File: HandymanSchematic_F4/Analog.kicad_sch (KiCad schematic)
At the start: 43 parts, among them Q1 2N7002, U2 TL074, U5 LM2904

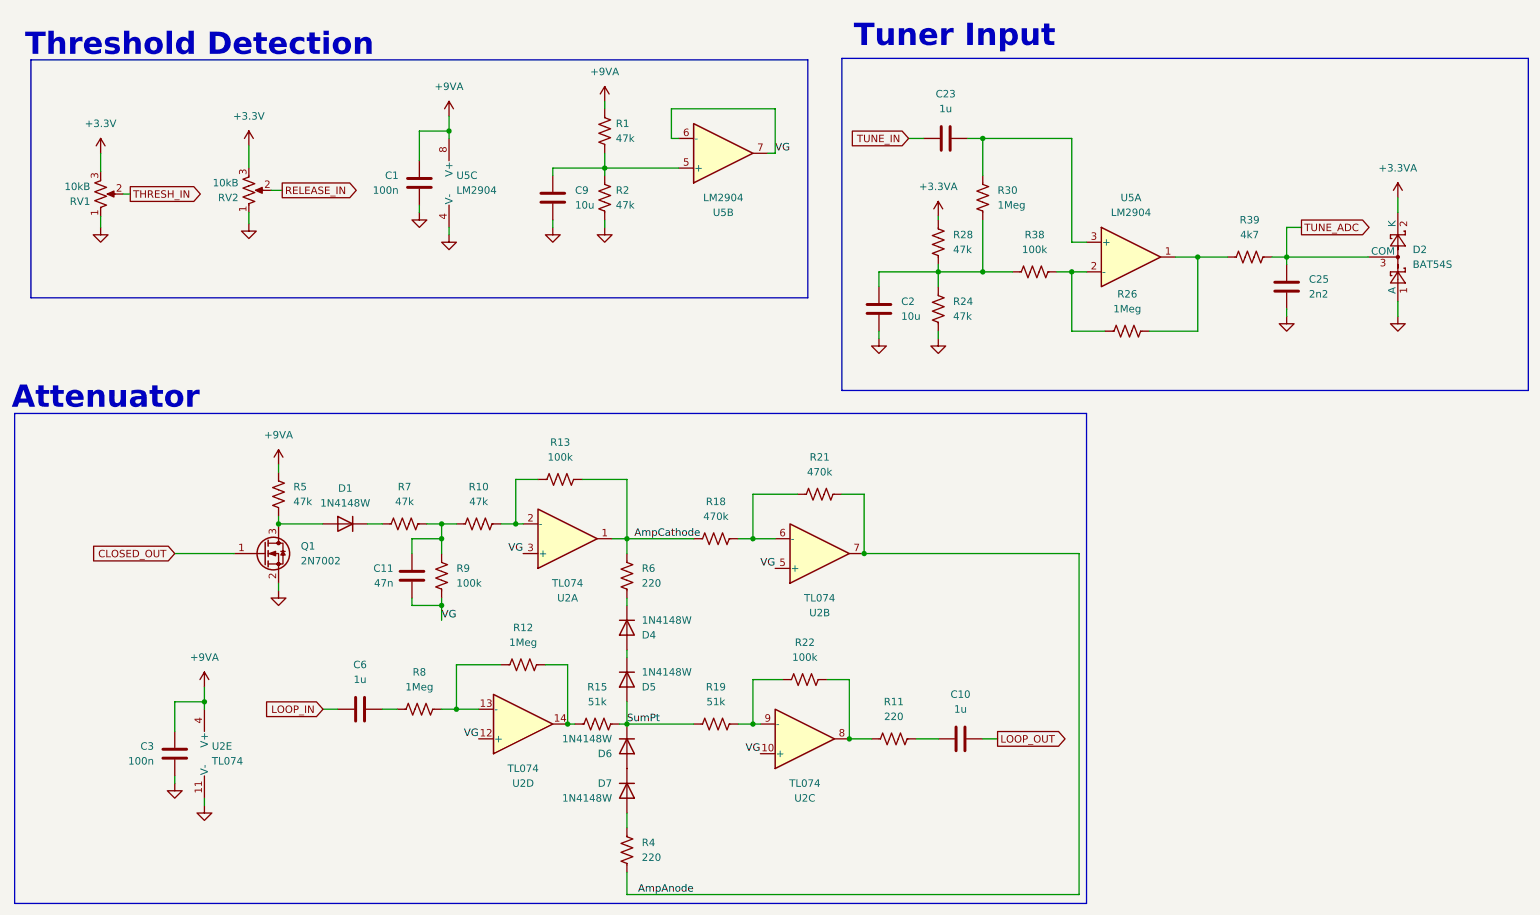
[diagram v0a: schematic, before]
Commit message: added anti-ringing caps, widened jack spacing a bit
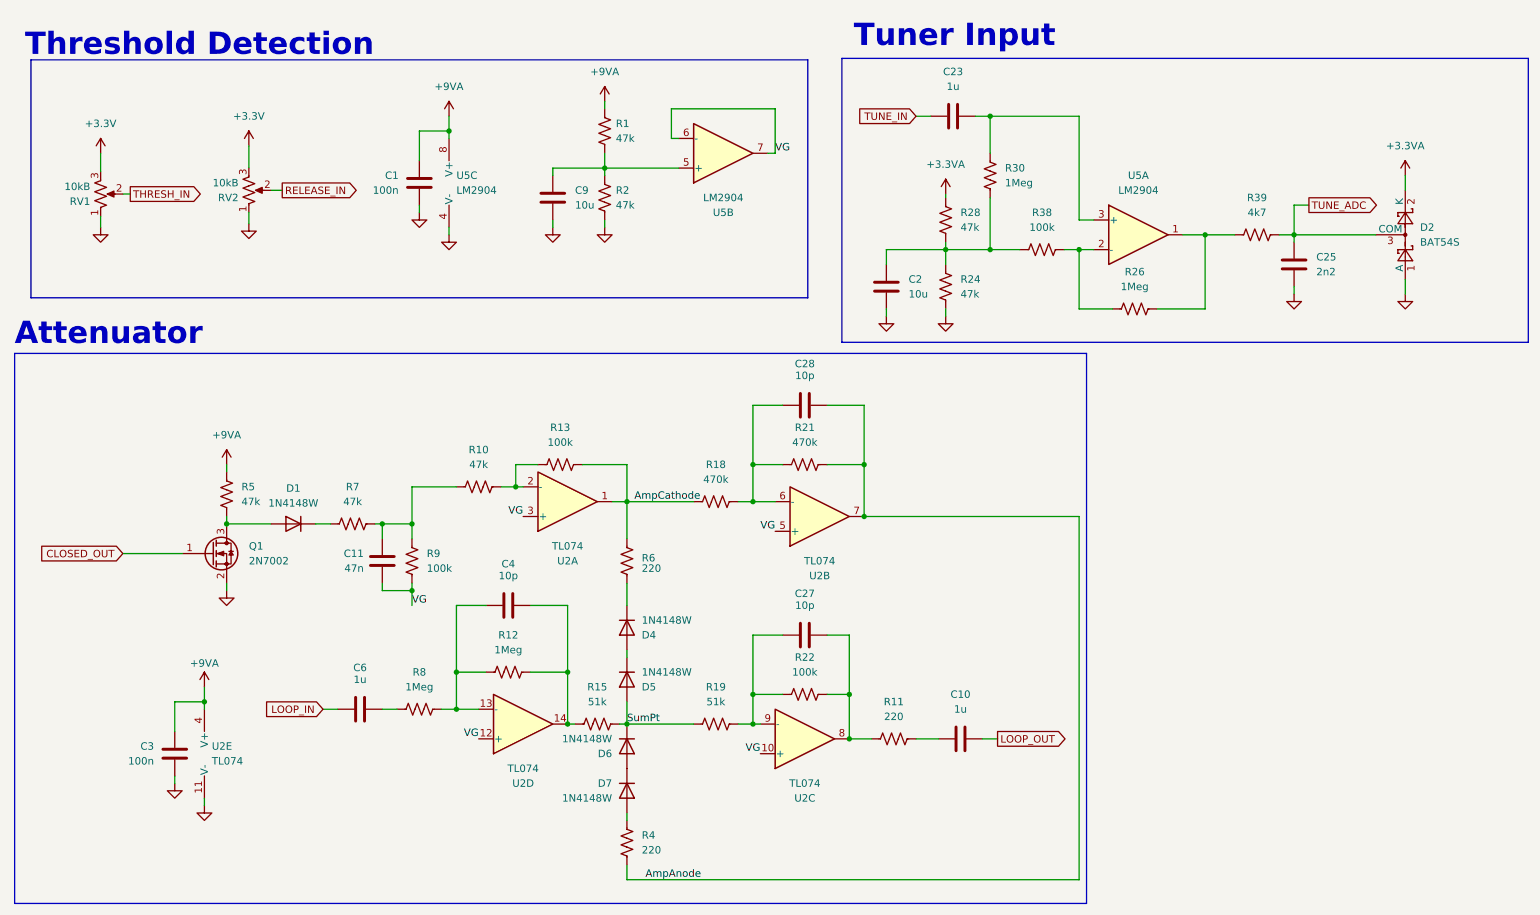
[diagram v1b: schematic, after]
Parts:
- added C27, C28, C4: 10p, Capacitor_SMD:C_0805_2012Metric, symbol Device:C
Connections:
- net AmpAnode: now also C28.2
- net at R19.2, R22.1, U2.9 (-): now also C27.1
- net at R18.2, R21.1, U2.6 (-): now also C28.1
- net at R12.1, R8.2, U2.13 (-): now also C4.1
- net at R12.2, R15.1, U2.14: now also C4.2
- net at R11.1, R22.2, U2.8: now also C27.2
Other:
- moved on the sheet: C11, C2, C23, C25, D1, D2, Q1, R10, R12, R13, R18, R21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

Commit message: added de-ringing caps
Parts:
- added C29: 10p, Capacitor_SMD:C_0805_2012Metric, symbol Device:C
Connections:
- net AmpCathode: now also C29.2
- net at R10.2, R13.1, U2.2 (-): now also C29.1
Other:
- moved on the sheet: C25, D2, R26, R39, U5A
